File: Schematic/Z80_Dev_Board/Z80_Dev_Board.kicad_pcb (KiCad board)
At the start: 2 copper layers, 120.7 x 98.3 mm, 45 parts, among them J1 MCU Interface, J2 MCU Interface 2, J3 Expansion port, J4 UART B, J5 UART A, J6 GPIO Input, J7 GPIO Output, U1 74AC08, U2 62256, U3 62256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

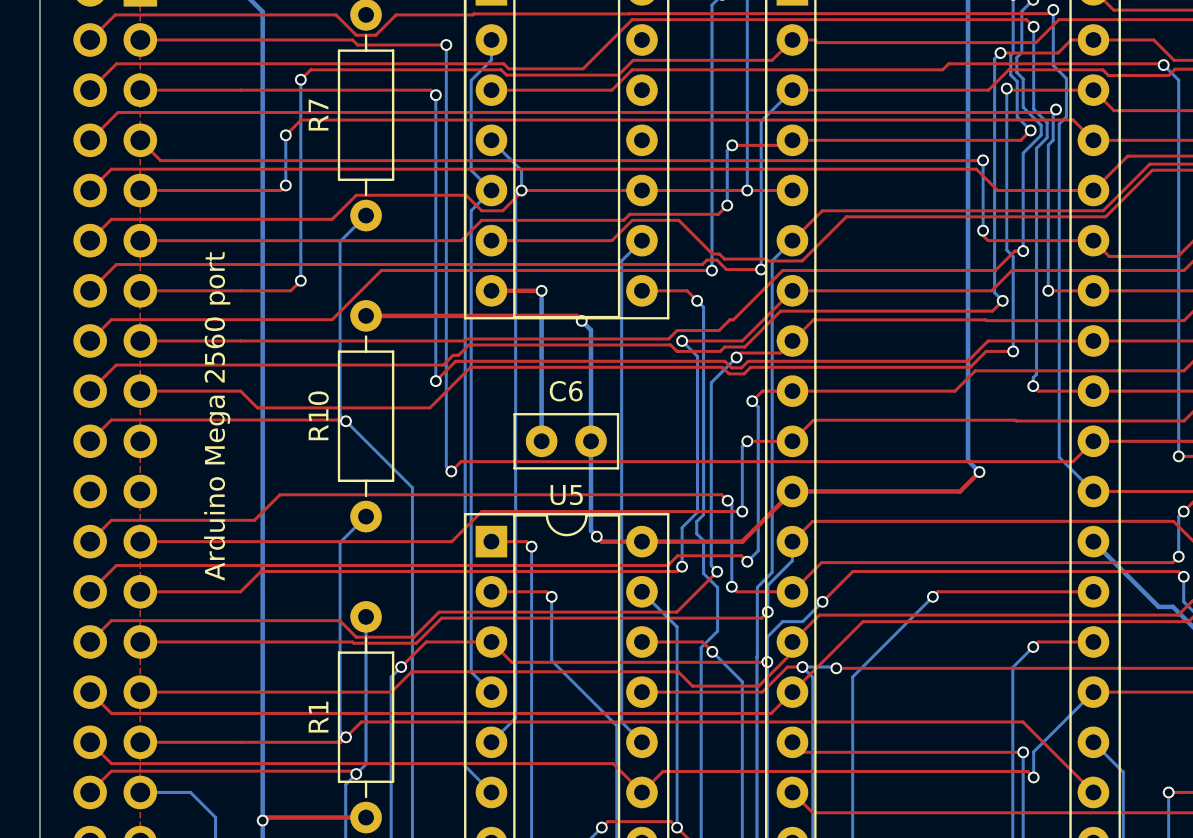
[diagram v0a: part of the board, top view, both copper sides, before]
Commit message: Replaced A15 by A07 in UART selection
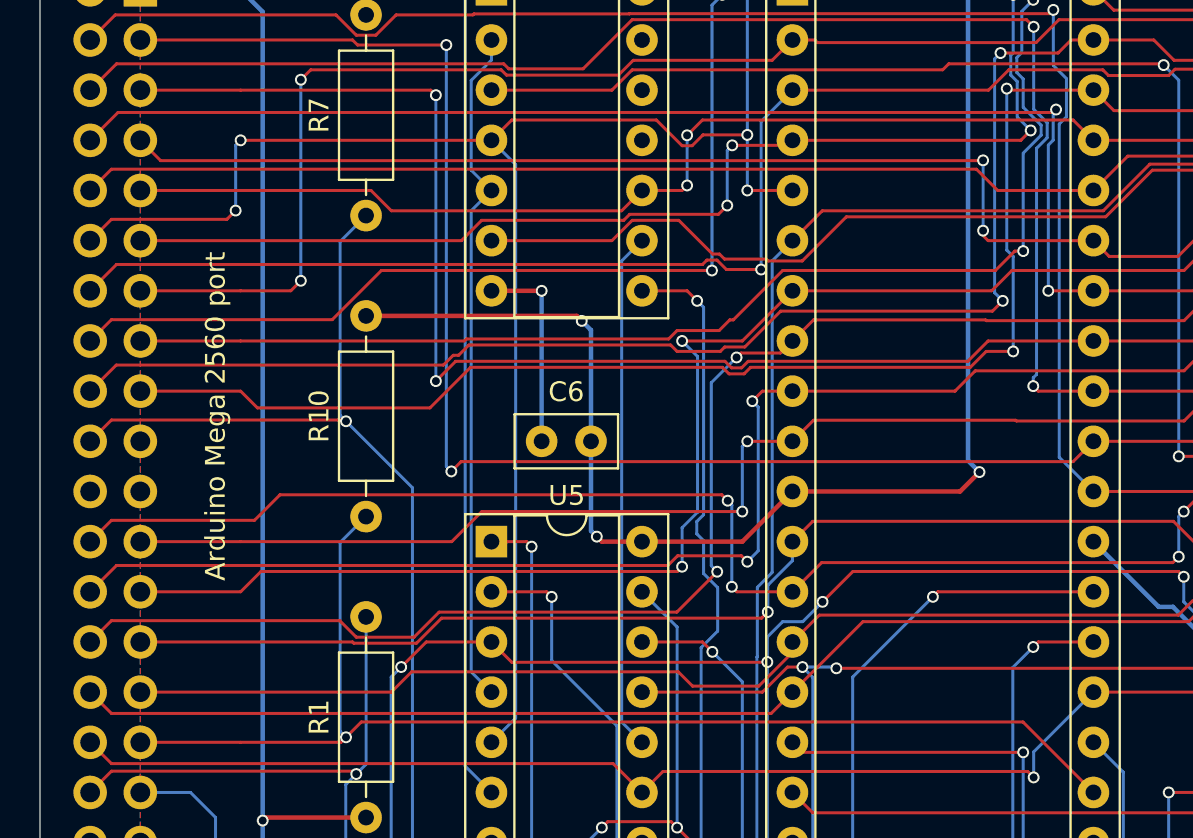
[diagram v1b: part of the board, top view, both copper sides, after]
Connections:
- U4 pad 10: a15 -> a7
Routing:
- net a15: track 200.9 -> 204.1 mm, vias 4 -> 6
- net a7: track 127.0 -> 127.8 mm
